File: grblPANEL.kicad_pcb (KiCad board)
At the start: 4 copper layers, 84 x 55 mm, 122 parts, among them J101 Conn_01x02, J201 2x5x1.27mm, J202 USB_C_Receptacle_USB2.0, J301 Conn_01x02, J401 Conn_01x02, J501 ILI9488, J601 Conn_02x10_Odd_Even, J701 Conn_01x04, J702 Conn_01x04, J703 Conn_01x04, J704 Conn_01x04, Q501 Q_NPN_BEC - S8050, SW201 SW_Push, SW202 SW_Push, U101 MAX17612A, U102 AZ1117-3.3, U201 STM32G0B1CxTxN, U202 USBLC6-2SC6, U301 SN65HVD230, U401 THVD1406, U601 ADP5589, Y201 8MHz

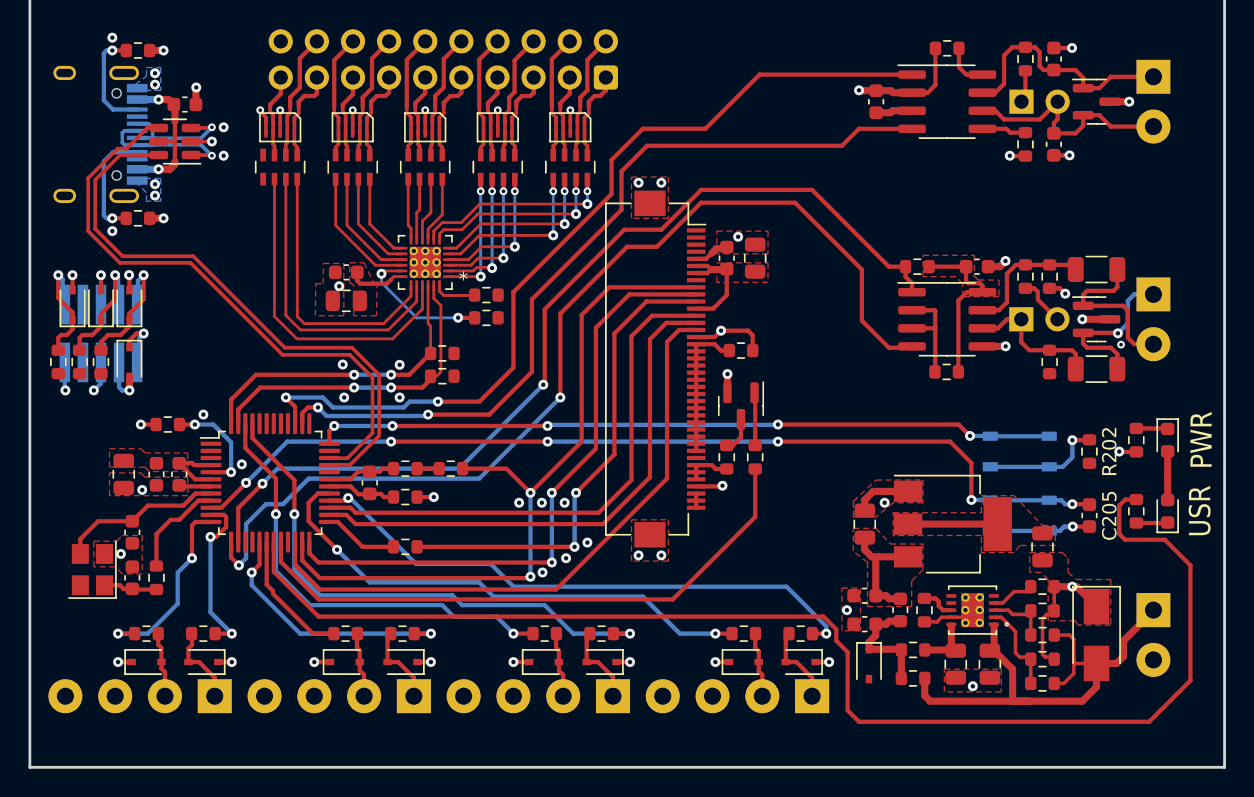
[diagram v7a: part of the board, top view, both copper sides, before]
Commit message: initial routing complete, pending test points & cleanup
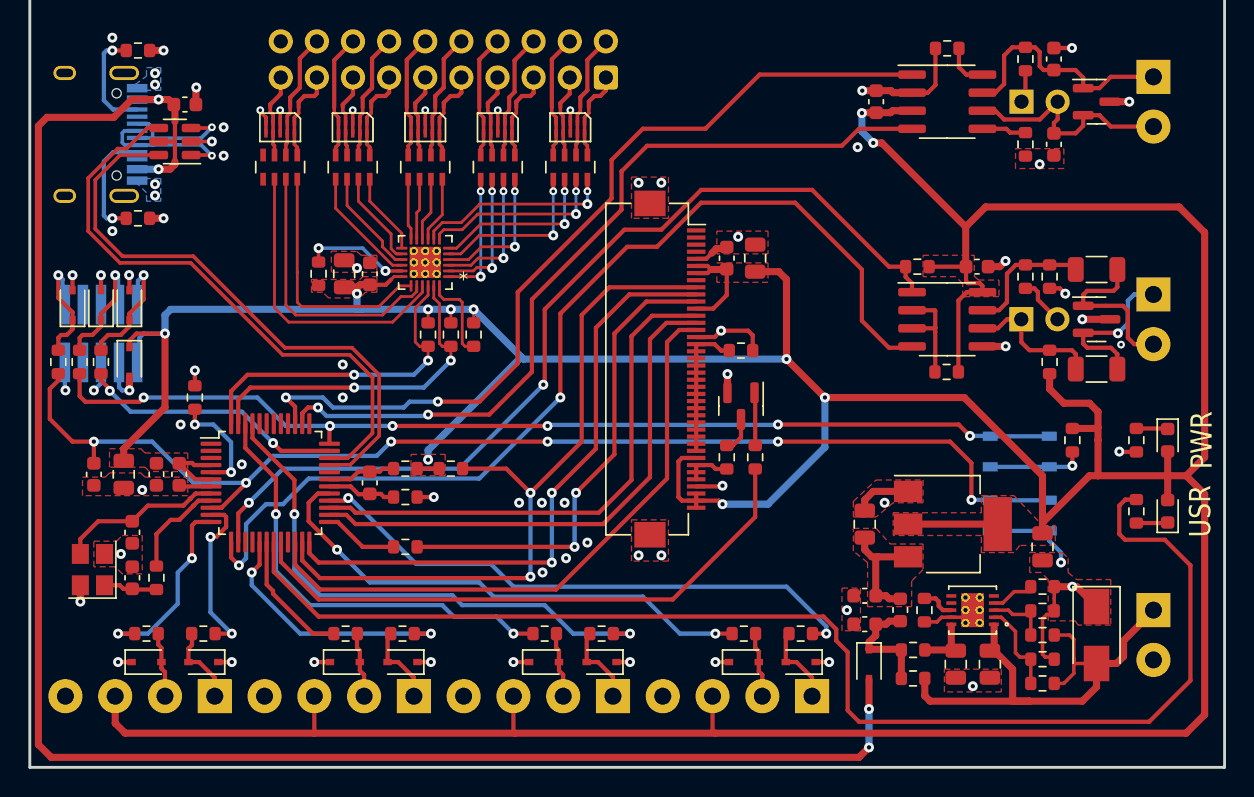
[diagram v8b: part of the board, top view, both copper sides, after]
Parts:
- moved C205 70.1 mm to (25.5, 163.4)
- moved R604 12.2 mm to (41.3, 149.3), turned to 90 degrees
- moved R602 2.99 mm to (50.6, 153.6), turned to -90 degrees
- moved R603 2.92 mm to (52.2, 153.6), turned to -90 degrees
- moved R201 2.69 mm to (32.6, 158.0), turned to -90 degrees
- moved C601 1.91 mm to (43.1, 149.3), turned to 90 degrees
- moved R601 1.66 mm to (49.0, 153.6), turned to -90 degrees
- moved C602 1.65 mm to (44.9, 149.3), turned to 90 degrees
- moved R202 1.44 mm to (94.3, 161.0), turned to 90 degrees
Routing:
- net +3V3: track 47.6 -> 354.4 mm, vias 1 -> 11
- net VBUS: track 10.9 -> 127.5 mm, vias 2 -> 4
- net /MCU/SWCLK/BOOT0: track 52.1 -> 72.5 mm, vias 5 -> 6
- net /MCU/SWDIO: track 0.00 -> 18.7 mm, vias 0 -> 2
- net /MCU/~{RST}: track 67.1 -> 84.7 mm
- net /Keypad/KEYPAD_INT: track 2.95 -> 6.24 mm
- net /Keypad/KEYPAD_RST: track 9.72 -> 7.49 mm
- net /Keypad/C10: track 23.2 -> 21.2 mm
- net /Keypad/C8: track 19.4 -> 17.4 mm
- net /Keypad/C9: track 21.1 -> 19.4 mm
- net Net-(R202-Pad1): track 8.46 -> 6.78 mm
- net GND: track 93.5 -> 91.8 mm, vias 73 -> 72
- net KEYPAD_SDA: track 21.9 -> 23.4 mm
- net KEYPAD_CLK: track 22.7 -> 23.9 mm
- net /Keypad/C7: track 9.06 -> 8.36 mm
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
